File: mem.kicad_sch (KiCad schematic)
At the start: 17 parts, among them U102 XC7A75T-1CSG324, U501 MT41J128M16JT-125, U502 TPS51206

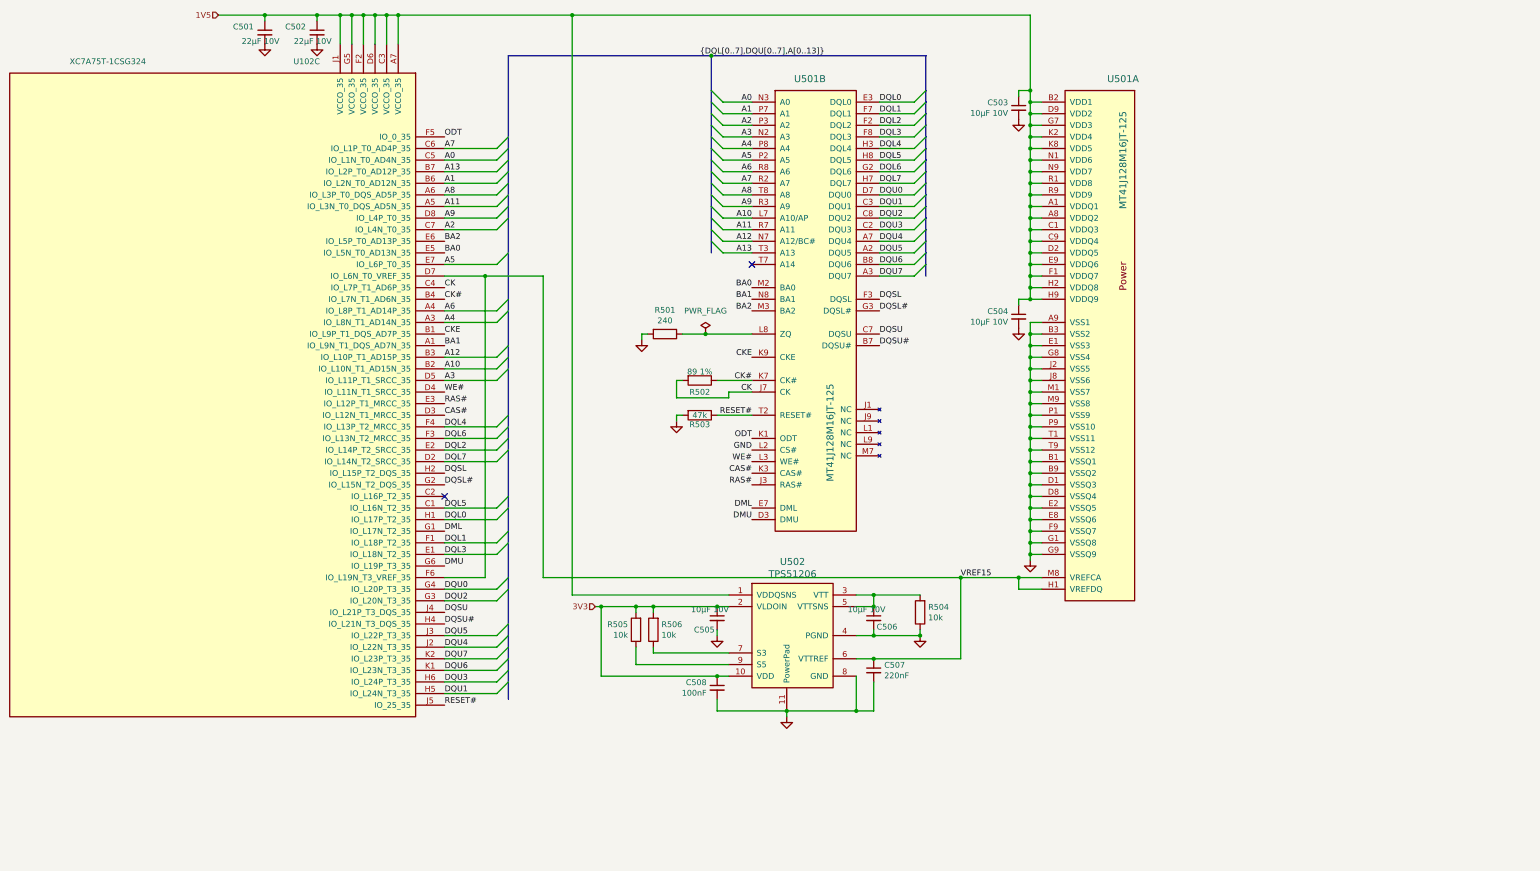
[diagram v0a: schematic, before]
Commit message: Cleaned up the directory and renamed files.  Also converted from the 324 package on the FPGA to the 484 package.  That conversion is still in-progress.
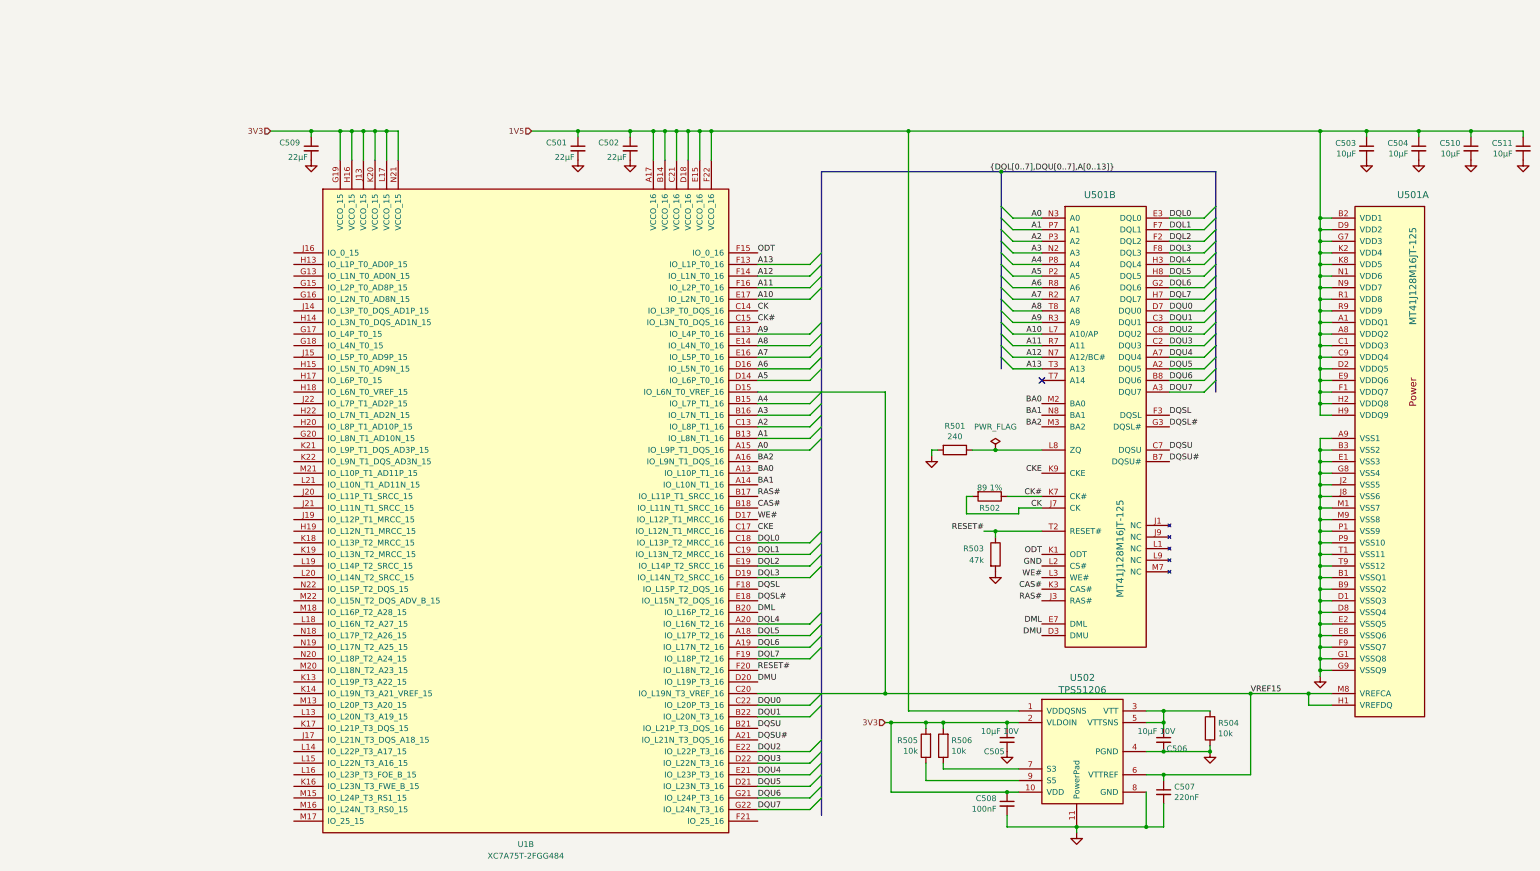
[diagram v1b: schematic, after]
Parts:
- removed U102: XC7A75T-1CSG324, Package_BGA:Xilinx_CSG324, symbol FPGA_Xilinx_Artix7:XC7A75T-CSG324
- added C509: 22µF, Capacitor_SMD:C_0603_1608Metric, symbol Device:C_Small
- added C510, C511: 10µF, Capacitor_SMD:C_0603_1608Metric, symbol Device:C_Small
- added U1: XC7A75T-2FGG484, Package_BGA:Xilinx_FGG484, symbol FPGA_Xilinx_Artix7:XC7A75T-FGG484
- C501, C502: value 22µF 10V -> 22µF; JLCPCB Part (none) -> C59461
- C503, C504: value 10µF 10V -> 10µF; JLCPCB Part (none) -> C85713
- C505, C506: JLCPCB Part (none) -> C85713
- R502: JLCPCB Part (none) -> C273787
- U502: JLCPCB Part (none) -> C88038; MPN TPS51206DSQT -> TPS51206DSQR
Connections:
- net 1V5: now also C510.1, C511.1, U1.A17 (VCCO_16), U1.B14 (VCCO_16), U1.C21 (VCCO_16), U1.D18 (VCCO_16), U1.E15 (VCCO_16), U1.F22 (VCCO_16)
- net 3V3: now also C509.1, U1.G19 (VCCO_15), U1.H16 (VCCO_15), U1.J13 (VCCO_15), U1.K20 (VCCO_15), U1.L17 (VCCO_15), U1.N21 (VCCO_15)
- net A0: now also U1.A15 (IO_L9P_T1_DQS_16)
- net A1: now also U1.B13 (IO_L8N_T1_16)
- net A10: now also U1.E17 (IO_L2N_T0_16)
- net A11: now also U1.F16 (IO_L2P_T0_16)
- net A12: now also U1.F14 (IO_L1N_T0_16)
- net A13: now also U1.F13 (IO_L1P_T0_16)
- net A2: now also U1.C13 (IO_L8P_T1_16)
- net A3: now also U1.B16 (IO_L7N_T1_16)
- net A4: now also U1.B15 (IO_L7P_T1_16)
- net A5: now also U1.D14 (IO_L6P_T0_16)
- net A6: now also U1.D16 (IO_L5N_T0_16)
- net A7: now also U1.E16 (IO_L5P_T0_16)
- net A8: now also U1.E14 (IO_L4N_T0_16)
- net A9: now also U1.E13 (IO_L4P_T0_16)
- net BA0: now also U1.A13 (IO_L10P_T1_16)
- net BA1: now also U1.A14 (IO_L10N_T1_16)
- net BA2: now also U1.A16 (IO_L9N_T1_DQS_16)
- net CAS#: now also U1.B18 (IO_L11N_T1_SRCC_16)
- net CK: now also U1.C14 (IO_L3P_T0_DQS_16)
- net CK#: now also U1.C15 (IO_L3N_T0_DQS_16)
- net CKE: now also U1.C17 (IO_L12N_T1_MRCC_16)
- net DML: now also U1.B20 (IO_L16P_T2_16)
- net DMU: now also U1.D20 (IO_L19P_T3_16)
- net DQL0: now also U1.C18 (IO_L13P_T2_MRCC_16)
- net DQL1: now also U1.C19 (IO_L13N_T2_MRCC_16)
- net DQL2: now also U1.E19 (IO_L14P_T2_SRCC_16)
- net DQL3: now also U1.D19 (IO_L14N_T2_SRCC_16)
- net DQL4: now also U1.A20 (IO_L16N_T2_16)
- net DQL5: now also U1.A18 (IO_L17P_T2_16)
- net DQL6: now also U1.A19 (IO_L17N_T2_16)
- net DQL7: now also U1.F19 (IO_L18P_T2_16)
- net DQSL: now also U1.F18 (IO_L15P_T2_DQS_16)
- net DQSL#: now also U1.E18 (IO_L15N_T2_DQS_16)
- net DQSU: now also U1.B21 (IO_L21P_T3_DQS_16)
- net DQSU#: now also U1.A21 (IO_L21N_T3_DQS_16)
- net DQU0: now also U1.C22 (IO_L20P_T3_16)
- net DQU1: now also U1.B22 (IO_L20N_T3_16)
- net DQU2: now also U1.E22 (IO_L22P_T3_16)
- net DQU3: now also U1.D22 (IO_L22N_T3_16)
- net DQU4: now also U1.E21 (IO_L23P_T3_16)
- net DQU5: now also U1.D21 (IO_L23N_T3_16)
- net DQU6: now also U1.G21 (IO_L24P_T3_16)
- net DQU7: now also U1.G22 (IO_L24N_T3_16)
- net GND: now also C509.2, C510.2, C511.2
- net ODT: now also U1.F15 (IO_0_16)
- net RAS#: now also U1.B17 (IO_L11P_T1_SRCC_16)
- net RESET#: now also U1.F20 (IO_L18N_T2_16)
- net VREF15: now also U1.C20 (IO_L19N_T3_VREF_16), U1.D15 (IO_L6N_T0_VREF_16)
- net WE#: now also U1.D17 (IO_L12P_T1_MRCC_16)
- no-connect marks 2 -> 1
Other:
- moved on the sheet: C501, C502, C503, C504, C505, C506, C507, C508, R501, R502, R503, R504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

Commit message: Switched the level converters to 74HCT2G04 and 75LVC2G04.  Still need to remap the FPGA pins to the signal odering.
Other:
- company: (none) -> Vintage Computer Enterprises
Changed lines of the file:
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@@
 	(title_block
 		(title "QSIC - QBUS Storage & I/O Card")
-		(date "2025-03-28")
+		(date "2025-04-12")
 		(rev "0.4")
+		(company "Vintage Computer Enterprises")
 	)
 	(junction
